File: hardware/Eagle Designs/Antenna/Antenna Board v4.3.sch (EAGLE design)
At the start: 20 parts, among them J1 5037630291, J10 MCX-J-P-X-ST-TH1, J11 U.FL-R-SMT-1(01), J12 MCX-J-P-X-ST-TH1, J13 MCX-J-P-X-ST-TH1, J14 UJ2-MIBH-G-SMT-TR, J15 MOLEX_503763-0491MOLEX_503763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, J16 ARJM11C7-104-AB-EW2, J2 503763-0591, J3 MOLEX_503763-0491MOLEX_503763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

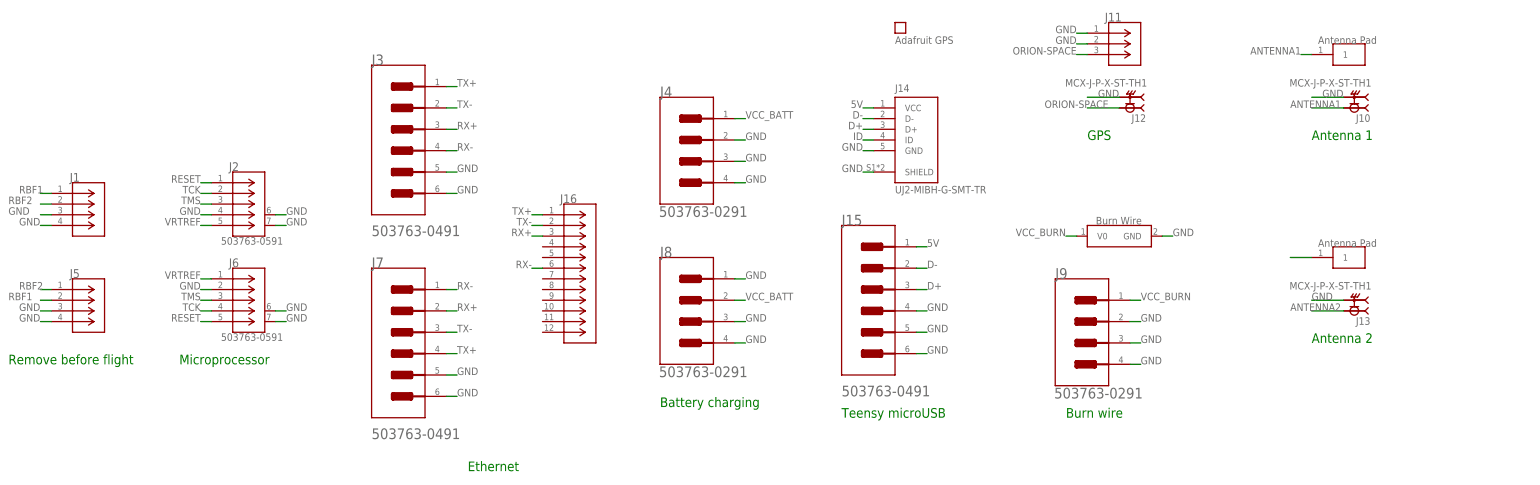
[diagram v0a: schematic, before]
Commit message: Antenna board edits
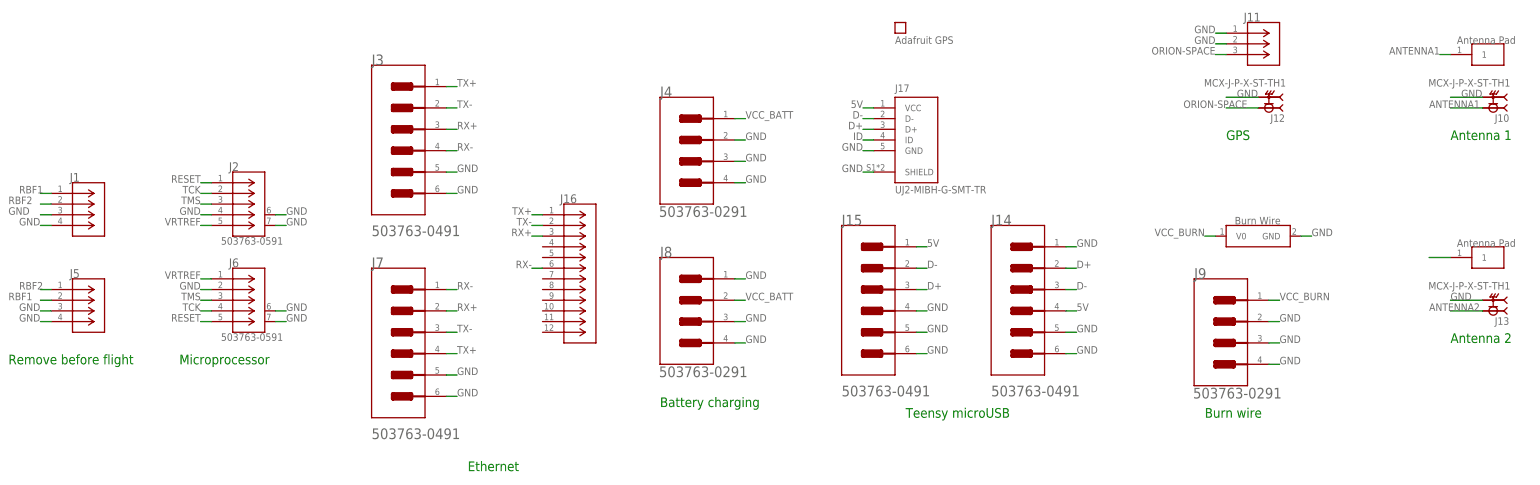
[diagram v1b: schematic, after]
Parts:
- added J17: UJ2-MIBH-G-SMT-TR, UJ2-MIBH-G-SMT-TR:UJ2-MIBH-G-SMT-TR
- J14: value UJ2-MIBH-G-SMT-TR -> MOLEX_503763-0491MOLEX_503763-0491_0_0; device UJ2-MIBH-G-SMT-TR:UJ2-MIBH-G-SMT-TR -> Molex - 503763-0491:MOLEX_503763-0491MOLEX_503763-0491_0_0
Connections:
- net 5V: now also J14.4, J17.VCC; no longer J14.VCC
- net D+: now also J14.2, J17.D+; no longer J14.D+
- net D-: now also J14.3, J17.D-; no longer J14.D-
- net GND: now also J14.1, J14.MNT_1, J14.MNT_2, J17.GND, J17.SHIELD; no longer J14.GND, J14.SHIELD
- net ID: now also J17.ID; no longer J14.ID
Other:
- moved on the sheet: J10, J11, J12, J13, J9
